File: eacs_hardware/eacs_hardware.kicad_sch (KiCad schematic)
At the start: 10 parts, among them Q1 S8050, U1 ESP32-WROOM-32

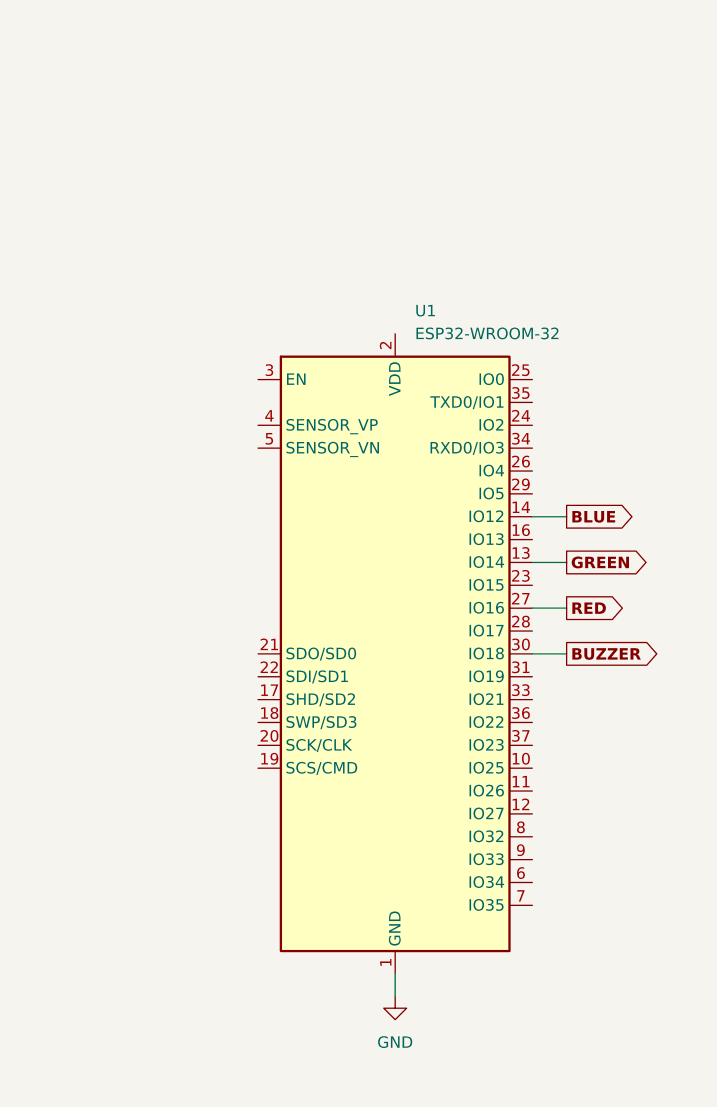
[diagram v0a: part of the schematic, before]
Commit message: Added Software, updated schematics
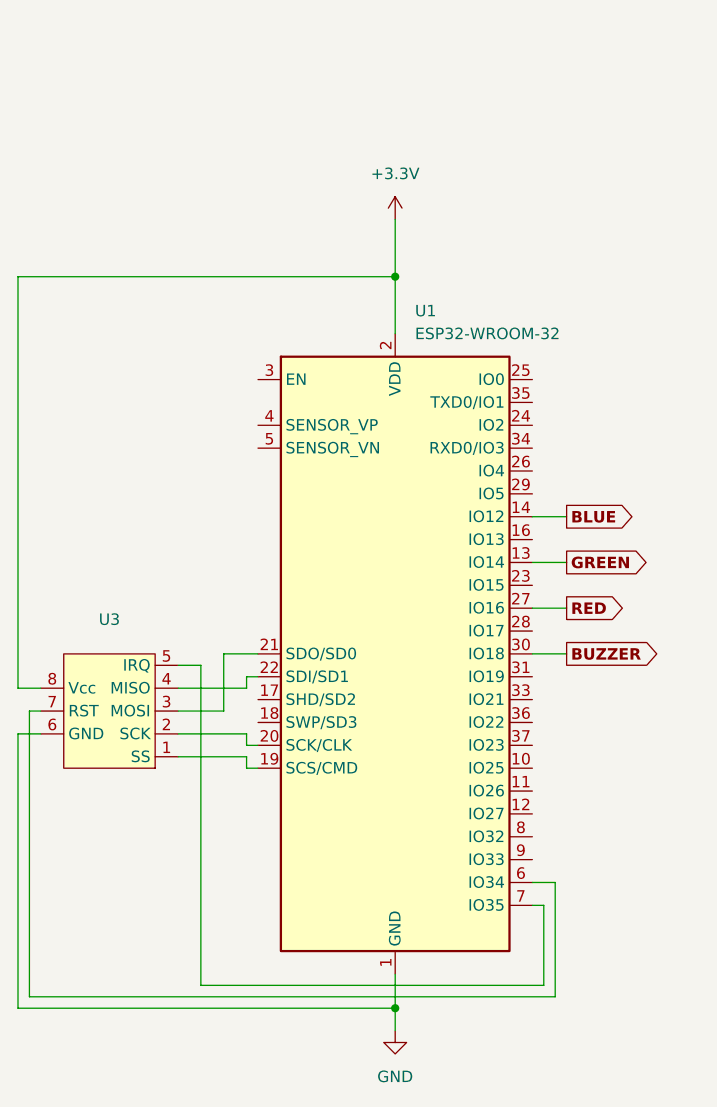
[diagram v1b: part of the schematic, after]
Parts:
- added U3: ~, symbol custom_components:RC522DB
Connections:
- net GND: now also U3.6 (GND)
- net at U1.19 (SCS/CMD): now also U3.1 (SS)
- net +3.3V: now reaches U1.2 (VDD)
- net +3.3V: now also U3.8 (Vcc)
- net at U1.20 (SCK/CLK): now also U3.2 (SCK)
- net at U1.21 (SDO/SD0): now also U3.3 (MOSI)
- net at U1.22 (SDI/SD1): now also U3.4 (MISO)
- net at U1.6 (IO34): now also U3.7 (RST)
- net at U1.7 (IO35): now also U3.5 (IRQ)

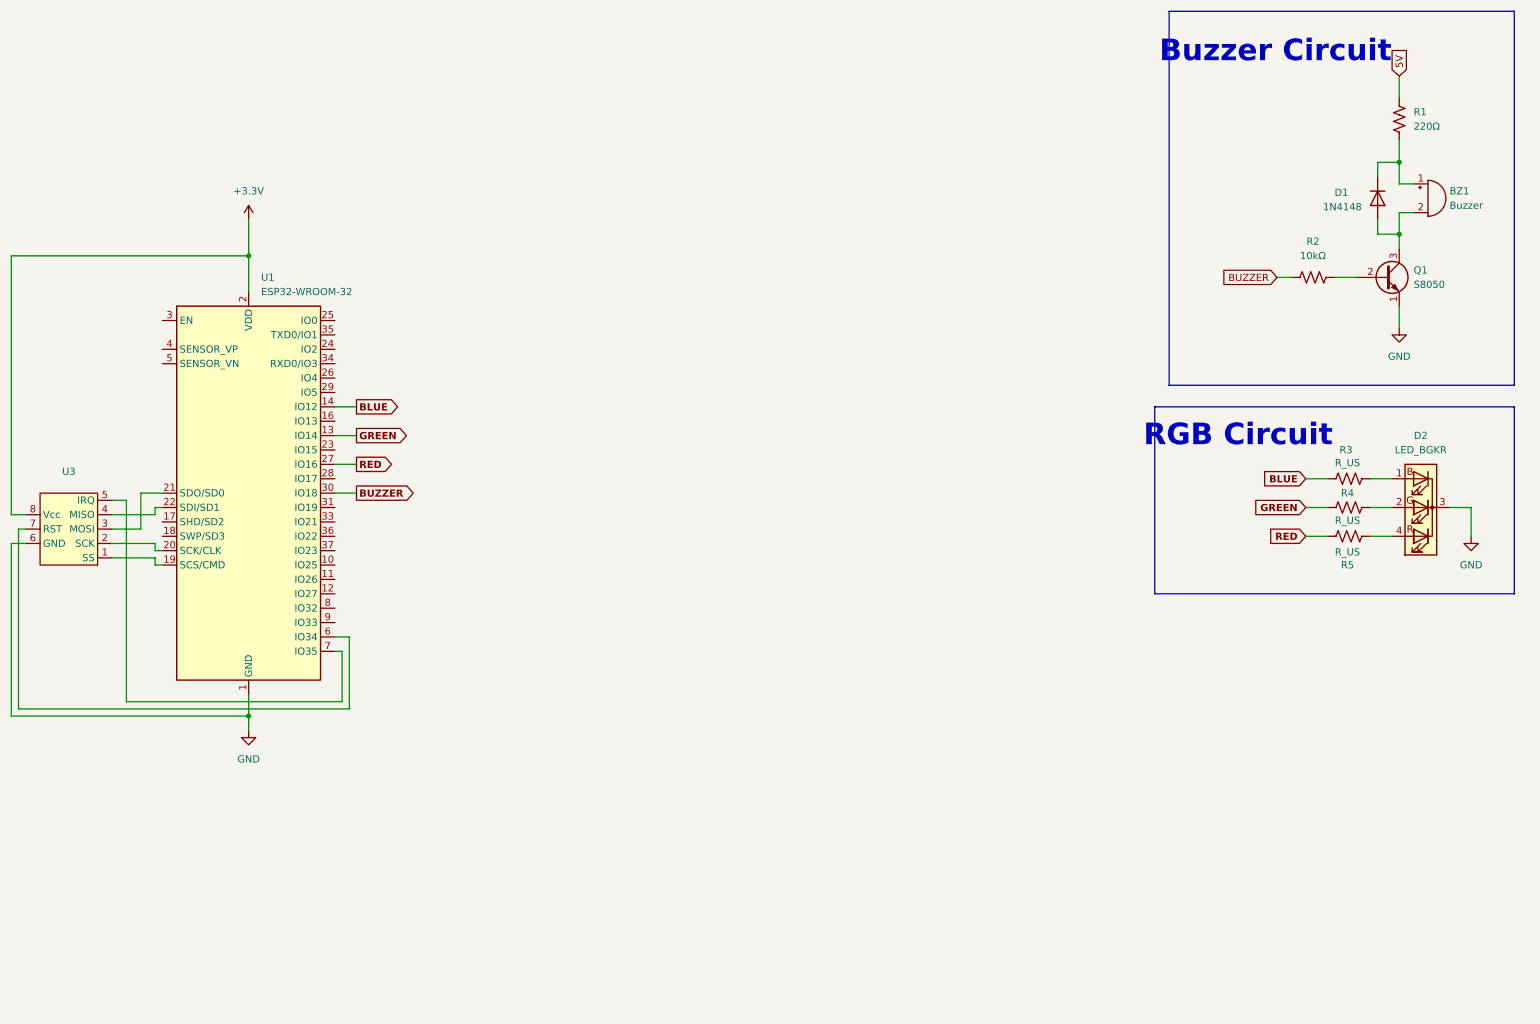
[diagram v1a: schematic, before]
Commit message: Finished ESP32 circuit
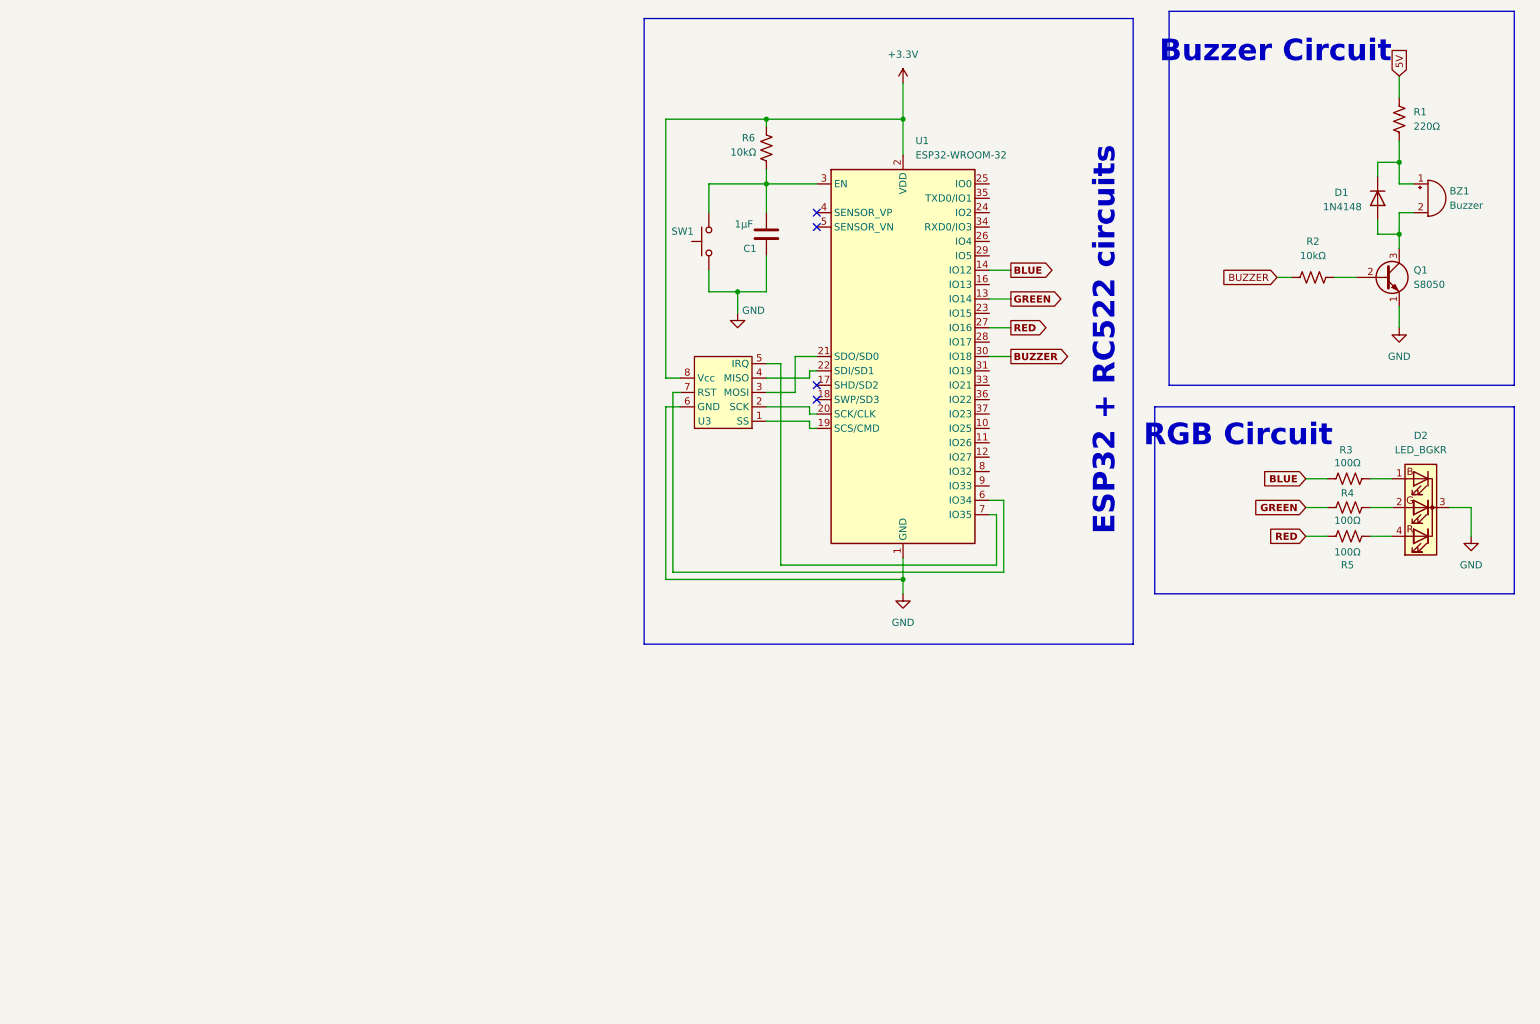
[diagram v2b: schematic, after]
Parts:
- added C1: 1µF, symbol Device:C
- added R6: 10kΩ, symbol Device:R_US
- added SW1: SW_Push, symbol Switch:SW_Push
- R3, R4, R5: value R_US -> 100Ω
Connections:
- net +3.3V: now also R6.1
- net GND: now also C1.2, SW1.1
- net at U1.3 (EN): now also C1.1, R6.2, SW1.2
- no-connect marks 0 -> 4
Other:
- note added: "ESP32 + RC522 circuits"
- moved on the sheet: U1, U3

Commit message: Almost done with 5V regulator
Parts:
- added D3: 1N4731A, Diode_THT:D_DO-41_SOD81_P10.16mm_Horizontal, symbol Diode:1N47xxA
- added Q2, Q3, Q4: SS8050, Package_TO_SOT_SMD:SOT-23, symbol Transistor_BJT:SS8050
- added R10: R_US, symbol Device:R_US
- added R11: 300Ω, symbol Device:R_US
- added R12: 20kΩ, symbol Device:R_US
- added R7, R9: 2kΩ, symbol Device:R_US
- added R8: 1kΩ, symbol Device:R_US
- added U4: TLV172IDCK, Package_TO_SOT_SMD:SOT-353_SC-70-5, symbol Amplifier_Operational:TLV172IDCK
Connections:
- net 5V: now also R8.1, U4.3 (-), U4.4
- net GND: now also D3.2 (A), R12.2, R7.2, U4.2 (V-)
- net +3.3V: no longer names the net of R6.1, U1.2 (VDD), U3.8 (Vcc)
- net +3.3V: now also R7.1, R8.2
- new net: Q2.1 (B), Q3.3 (C), Q4.3 (C), R9.2
- new net: Q2.2 (E), Q3.1 (B), R10.1
- new net: Q4.1 (B), R11.2, R12.1
- new net: D3.1 (K), Q4.2 (E)
- new net: Q3.2 (E), R10.2, R11.1, U4.1 (+)
- new net 20V: Q2.3 (C), R9.1, U4.5 (V+)
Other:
- note added: "5V Regulator"
- note added: "ESP32 EACS"
- moved on the sheet: BZ1, C1, D1, D2, Q1, R1, R2, R3, R4, R5, R6, SW1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
